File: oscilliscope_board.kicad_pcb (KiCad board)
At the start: 4 copper layers, 34 parts, among them J1 Conn_Coaxial, J2 Conn_Coaxial, SW1 SW_Push, SW2 RotaryEncoder_Switch_MP, U2 ADC0832

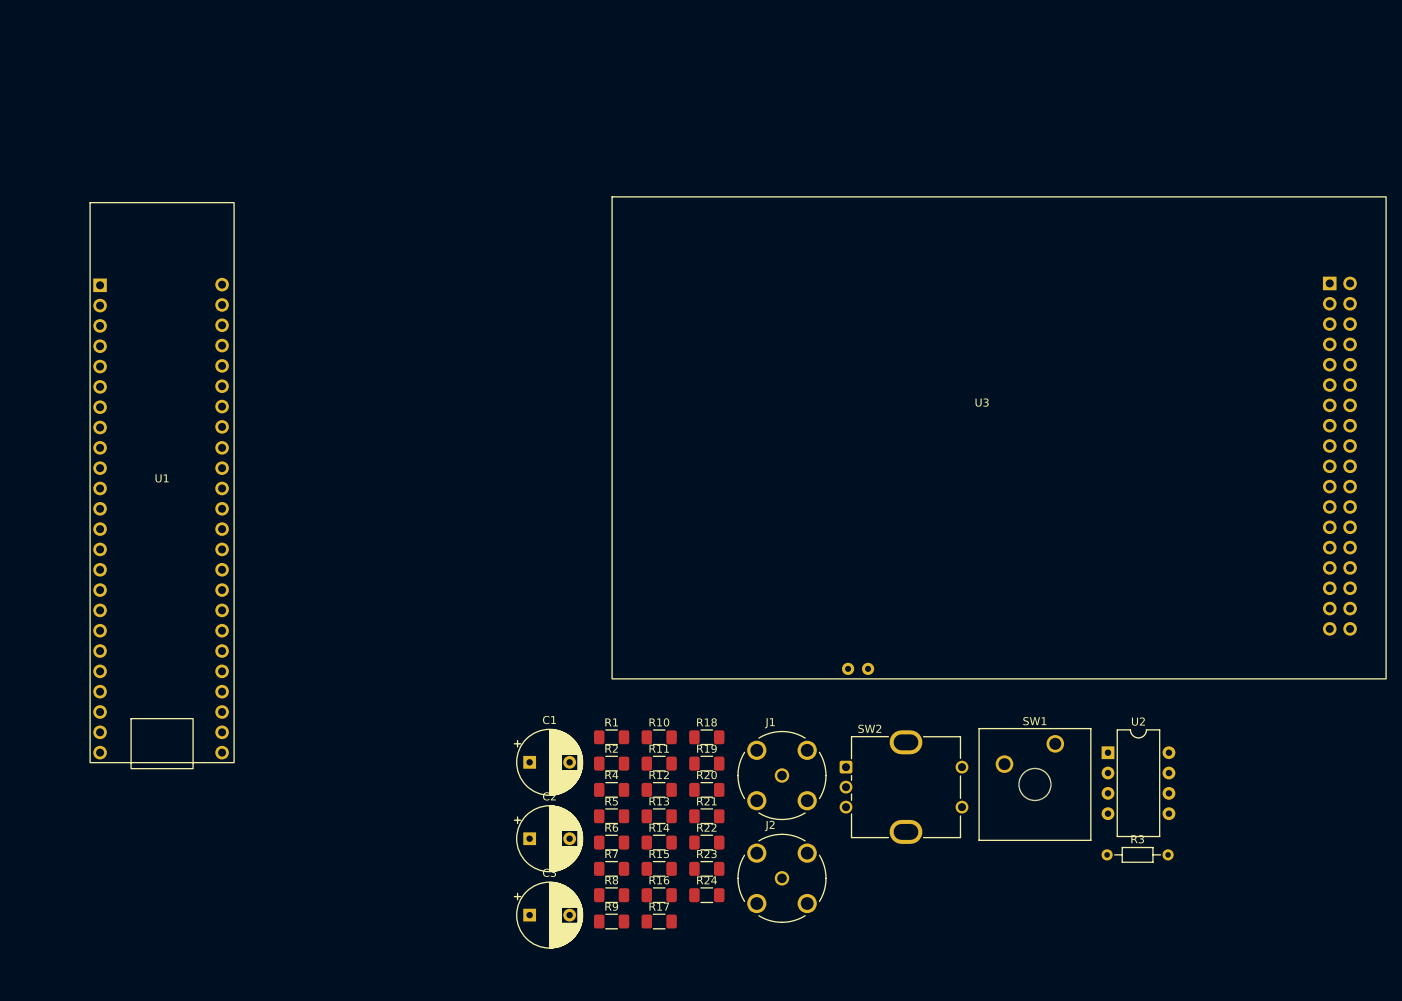
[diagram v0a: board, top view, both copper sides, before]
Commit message: routed all board connections. needs review
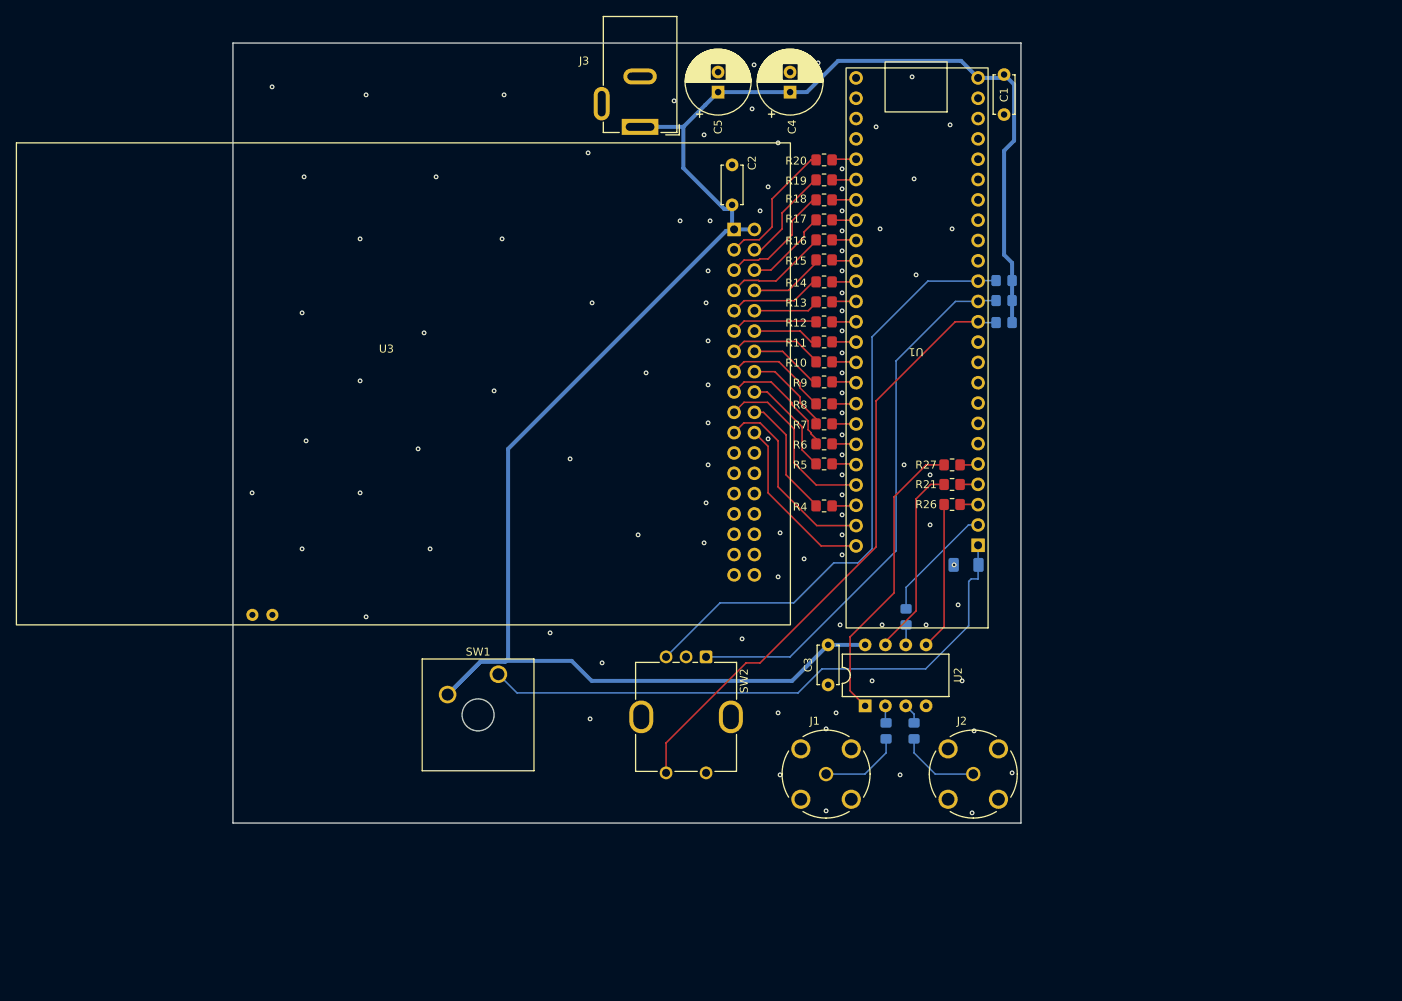
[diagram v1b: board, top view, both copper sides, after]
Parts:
- added C4: 100uF, Capacitor_THT:CP_Radial_D8.0mm_P2.50mm, F.Cu at (130.5, 34.9)
- added C5: 100uF, Capacitor_THT:CP_Radial_D8.0mm_P2.50mm, F.Cu at (121.5, 34.9)
- added J3: Barrel_Jack, Connector_BarrelJack:BarrelJack_GCT_DCJ200-10-A_Horizontal, F.Cu at (111.8, 39.2)
- added R25: 33, Resistor_SMD:R_0805_2012Metric_Pad1.20x1.40mm_HandSolder, B.Cu at (145.0, 100.5)
- added R26: 33, Resistor_SMD:R_0805_2012Metric_Pad1.20x1.40mm_HandSolder, F.Cu at (150.8, 86.5)
- added R27: 33, Resistor_SMD:R_0805_2012Metric_Pad1.20x1.40mm_HandSolder, F.Cu at (150.8, 81.5)
- C1, C2, C3: footprint Capacitor_THT:CP_Radial_D8.0mm_P5.00mm -> Capacitor_THT:C_Disc_D4.7mm_W2.5mm_P5.00mm
- R1, R2, R22, R23, R24: footprint Resistor_SMD:R_1206_3216Metric_Pad1.30x1.75mm_HandSolder -> Resistor_SMD:R_0805_2012Metric_Pad1.20x1.40mm_HandSolder; moved to B.Cu
- R10, R11, R12, R13, R14, R15, R16, R17, R18, R19, R20, R21, R4, R5, R6, R7, R8, R9: footprint Resistor_SMD:R_1206_3216Metric_Pad1.30x1.75mm_HandSolder -> Resistor_SMD:R_0805_2012Metric_Pad1.20x1.40mm_HandSolder
- R3: footprint Resistor_THT:R_Axial_DIN0204_L3.6mm_D1.6mm_P7.62mm_Horizontal -> Resistor_SMD:R_1206_3216Metric_Pad1.30x1.75mm_HandSolder; moved to B.Cu
- moved C1 104.4 mm to (157.2, 32.7), turned to -90 degrees
- moved U1 95.7 mm to (146.2, 66.9), turned to 180 degrees
- moved R17 90.1 mm to (134.8, 50.9), turned to 180 degrees
- moved R16 84.5 mm to (134.8, 53.4), turned to 180 degrees
- moved C2 83.2 mm to (123.2, 49.0), turned to 90 degrees
- moved R23 82.4 mm to (157.2, 58.5), turned to 180 degrees
- moved R24 80.7 mm to (157.2, 63.7), turned to 180 degrees
- moved R20 80.1 mm to (134.8, 43.4), turned to 180 degrees
- moved R15 78.9 mm to (134.8, 55.9), turned to 180 degrees
- moved R22 77.3 mm to (157.2, 61.0), turned to 180 degrees
- moved U3 74.8 mm to (80.0, 67.5)
- moved R19 74.4 mm to (134.8, 45.9), turned to 180 degrees
- moved R14 73.0 mm to (134.8, 58.6), turned to 180 degrees
- moved R9 72.5 mm to (134.8, 71.1), turned to 180 degrees
- moved SW1 70.2 mm to (94.0, 107.7)
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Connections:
- C1 pad 2: GNDD -> GNDA
- C2 pad 2: GNDD -> GNDA
- C3 pad 2: GNDD -> GNDA
- R21 pad 2: Net-(U1-PIO2) -> Net-(U1-PIO4)
- R3 pad 1: GNDD -> GNDA
- SW2 pad C: GNDD -> GNDA
- SW2 pad S1: GNDD -> GNDA
- U1 pad 25: GNDD -> GNDA
- U2 pad 1: Net-(U1-PIO5) -> Net-(U2-CS)
- U2 pad 4: GNDD -> GNDA
- U2 pad 5: Net-(U1-PIO4) -> Net-(U2-DIN)
- U2 pad 6: Net-(U1-PIO3) -> Net-(U2-DOUT)
- U3 pad 35: GNDD -> GNDA
- U3 pad 36: GNDD -> GNDA
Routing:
- net +5V: track 0.00 -> 234.2 mm
- net Net-(U1-PIO12): track 0.00 -> 77.5 mm
- net Net-(U1-PIO14): track 0.00 -> 76.3 mm
- net Net-(U1-PIO1): track 0.00 -> 74.3 mm
- net Net-(U1-PIO13): track 0.00 -> 68.6 mm
- net Net-(U2-CS): track 0.00 -> 37.1 mm
- net Net-(U1-PIO47): track 0.00 -> 24.4 mm
- net Net-(U2-CLK): track 0.00 -> 24.1 mm
- net Net-(U1-PIO45): track 0.00 -> 22.5 mm
- net Net-(U1-PIO48): track 0.00 -> 22.0 mm
- net Net-(U2-DIN): track 0.00 -> 18.5 mm
- net Net-(U3-DB8): track 0.00 -> 17.0 mm
- net Net-(U3-WR): track 0.00 -> 15.6 mm
- net Net-(U3-DB1): track 0.00 -> 15.2 mm
- net Net-(U1-PIO2): track 0.00 -> 14.9 mm
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- added copper zone on In1.Cu, net GNDA
- added copper zone on In2.Cu, net GNDA
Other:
- board outline added: 98.5 x 97.5 mm

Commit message: added version to silkscreen, minor adustments
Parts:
- moved C1 27.6 mm to (176.0, 53.0)
- moved C2 27.6 mm to (142.0, 69.2)
- moved C3 27.6 mm to (154.0, 124.2)
- moved C4 27.6 mm to (149.2, 55.2)
- moved C5 27.6 mm to (140.2, 55.2)
- moved J1 27.6 mm to (153.8, 140.4)
- moved J2 27.6 mm to (172.2, 140.4)
- moved J3 27.6 mm to (130.5, 59.5)
- moved R1 27.6 mm to (161.2, 135.0)
- moved R10 27.6 mm to (153.5, 88.9)
- moved R11 27.6 mm to (153.5, 86.4)
- moved R2 27.6 mm to (164.8, 135.0)
- moved R20 27.6 mm to (153.5, 63.6)
- moved R21 27.6 mm to (169.5, 104.2)
- moved R25 27.6 mm to (163.8, 120.8)
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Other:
- board text added: "[ oscilliscope_board: v1.0 ]"
